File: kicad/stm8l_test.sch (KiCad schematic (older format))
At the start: 60 parts, among them J1 Conn_01x04, Q1 SI2365EDS-T1-GE3, Q2 2N7002, Q3 SI2365EDS-T1-GE3, Q4 SI2365EDS-T1-GE3, Q5 SI2365EDS-T1-GE3, Q6 SI2365EDS-T1-GE3, Q7 SI2365EDS-T1-GE3, Q8 SI2365EDS-T1-GE3, SW1 prog_sw, SW2 SW_Push, SW3 Rotary_Encoder_Switch, U1 BD70522GUL-E2, U2 STM8L101F3P

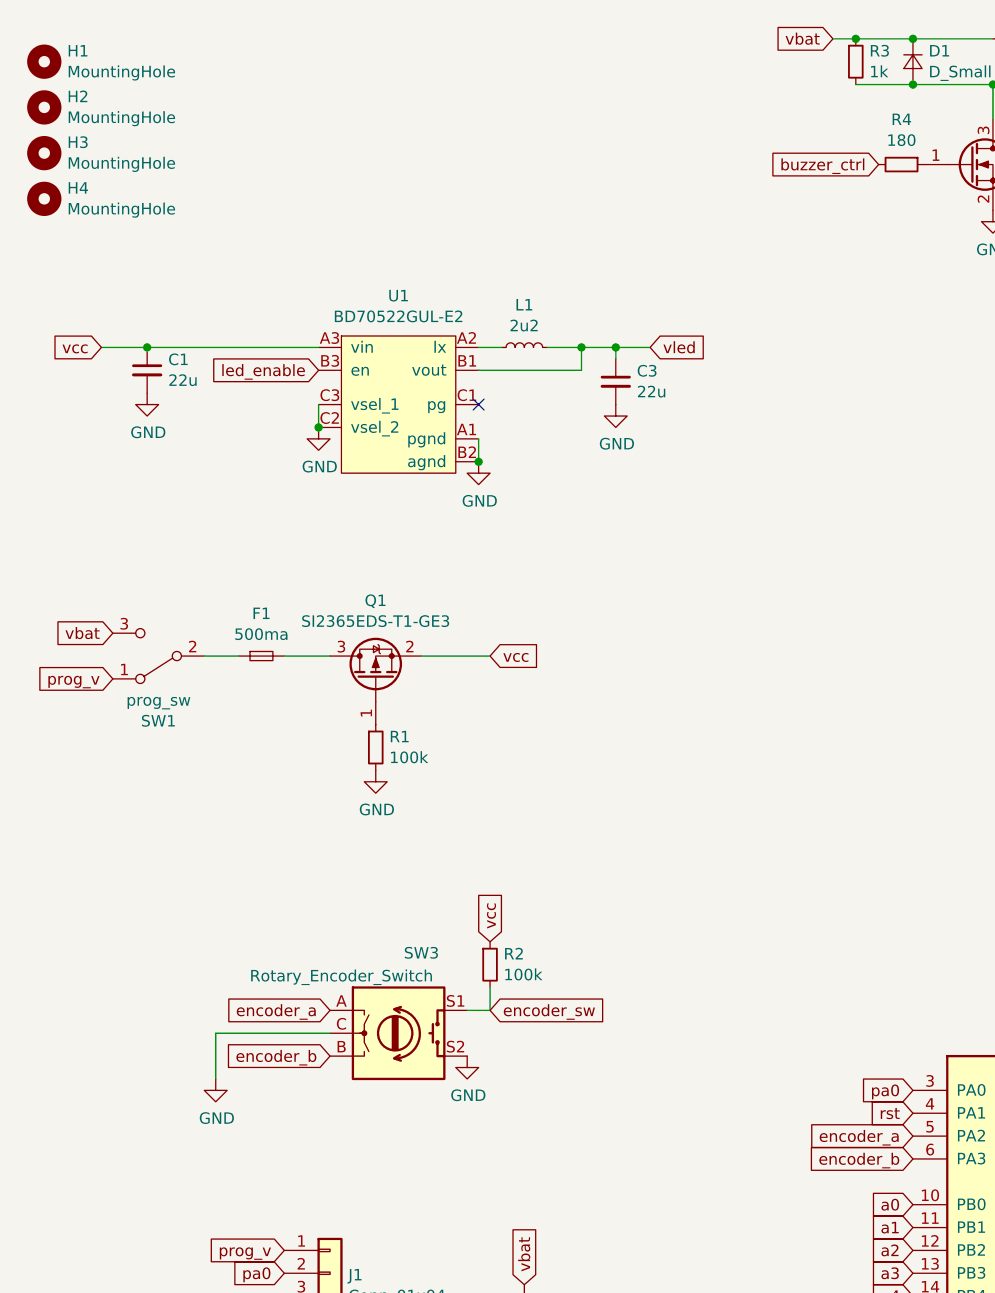
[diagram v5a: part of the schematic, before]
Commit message: Leds and buzzer works
added debounce caps
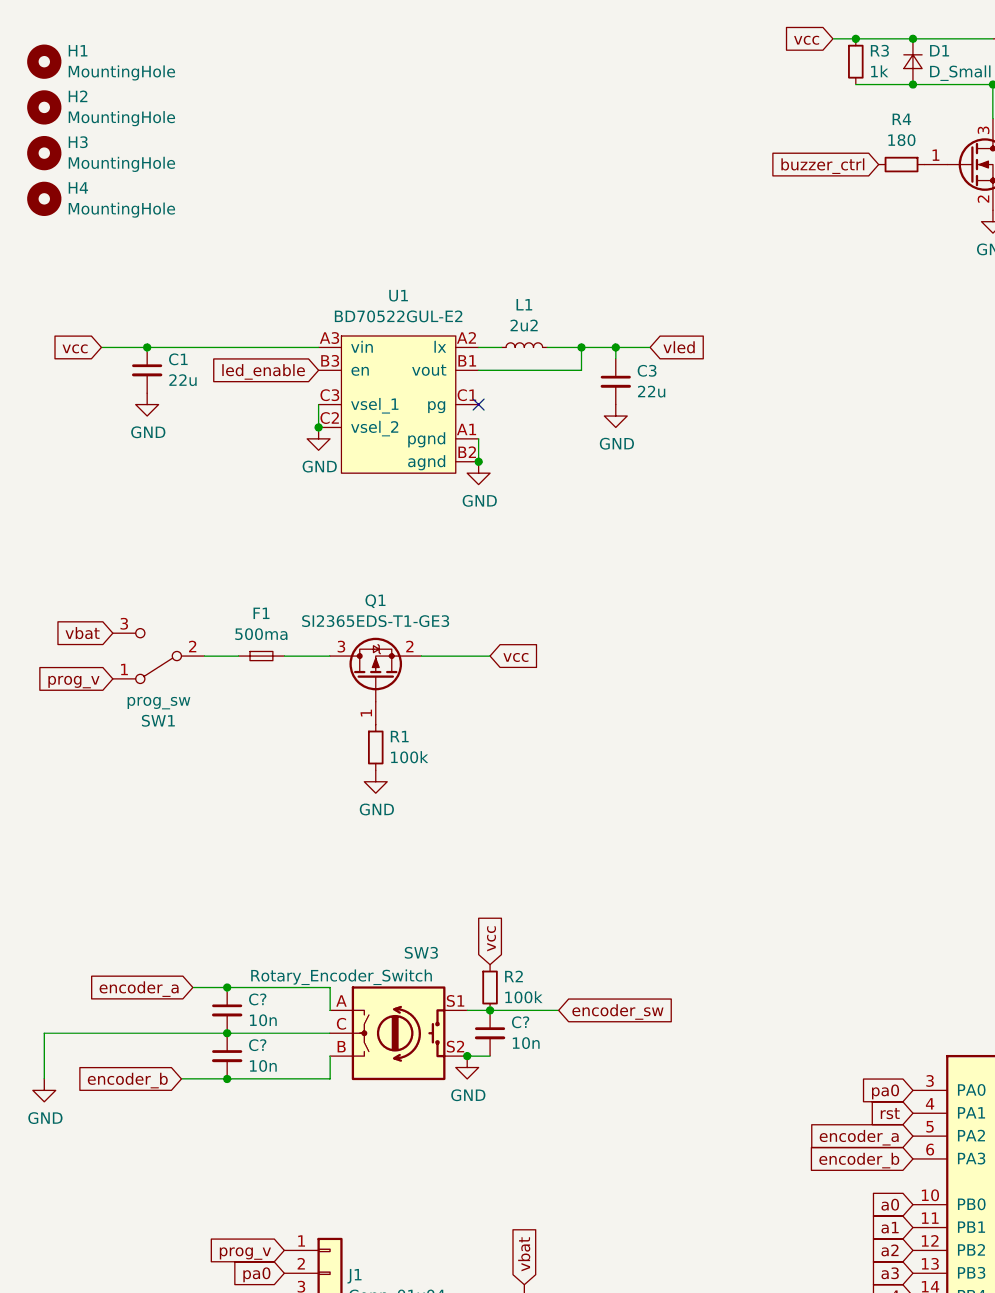
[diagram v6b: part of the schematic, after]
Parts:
- added C? (x3): 10n, symbol Device:C_Small
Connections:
- net GND: now also C?.1, C?.2, C?.2
- net encoder_a: now also C?.1
- net encoder_b: now also C?.2
- net encoder_sw: now also C?.1
- net vbat: no longer BZ1.1 (-), D1.1 (K), R3.1
- net vcc: now also BZ1.1 (-), D1.1 (K), R3.1
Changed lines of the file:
@@
 L power:GND #PWR02
 U 1 1 60746B0D
-P 1950 5250
-F 0 "#PWR02" H 1950 5000 50  0001 C CNN
-F 1 "GND" H 1955 5077 50  0000 C CNN
-F 2 "" H 1950 5250 50  0001 C CNN
-F 3 "" H 1950 5250 50  0001 C CNN
-	1    1950 5250
-	1    0    0    -1
-$EndComp
-Text GLabel 2450 5150 0    50   Input ~ 0
+P 1200 5250
+F 0 "#PWR02" H 1200 5000 50  0001 C CNN
+F 1 "GND" H 1205 5077 50  0000 C CNN
+F 2 "" H 1200 5250 50  0001 C CNN
+F 3 "" H 1200 5250 50  0001 C CNN
+	1    1200 5250
+	1    0    0    -1
+$EndComp
+Text GLabel 1800 5250 0    50   Input ~ 0
 encoder_b
-Text GLabel 2450 4950 0    50   Input ~ 0
+Text GLabel 1850 4850 0    50   Input ~ 0
 encoder_a
 Wire Wire Line
-	2450 5050 1950 5050
-Wire Wire Line
-	1950 5050 1950 5250
+	1200 5050 1200 5250
 $Comp
 L Device:Buzzer BZ1
@@
 	1    0    0    -1
 $EndComp
-Text GLabel 4650 700  0    50   Input ~ 0
-vbat
 Connection ~ 7900 1800
 Wire Wire Line
@@
 Wire Wire Line
 	6600 700  6800 700
-$Comp
-L Device:R_Small R2
-U 1 1 60B9FE81
-P 3150 4750
-F 0 "R2" H 3209 4796 50  0000 L CNN
-F 1 "100k" H 3209 4705 50  0000 L CNN
-F 2 "Resistor_SMD:R_0603_1608Metric_Pad1.05x0.95mm_HandSolder" H 3150 4750 50  0001 C CNN
-F 3 "~" H 3150 4750 50  0001 C CNN
-	1    3150 4750
-	1    0    0    -1
-$EndComp
-Text GLabel 3150 4650 1    50   Input ~ 0
-vcc
-Wire Wire Line
-	3150 4850 3150 4950
-Wire Wire Line
-	3150 4950 3050 4950
-Text GLabel 3150 4950 2    50   Input ~ 0
-encoder_sw
 Text GLabel 5000 6400 0    50   Input ~ 0
 encoder_sw
@@
 Wire Wire Line
 	2850 3400 3150 3400
+$Comp
+L Device:C_Small C?
+U 1 1 61046CCB
+P 2000 4950
+F 0 "C?" H 2092 4996 50  0000 L CNN
+F 1 "10n" H 2092 4905 50  0000 L CNN
+F 2 "" H 2000 4950 50  0001 C CNN
+F 3 "~" H 2000 4950 50  0001 C CNN
+	1    2000 4950
+	1    0    0    -1
+$EndComp
+$Comp
+L Device:C_Small C?
+U 1 1 61057664
+P 2000 5150
+F 0 "C?" H 2092 5196 50  0000 L CNN
+F 1 "10n" H 2092 5105 50  0000 L CNN
+F 2 "" H 2000 5150 50  0001 C CNN
+F 3 "~" H 2000 5150 50  0001 C CNN
+	1    2000 5150
+	1    0    0    -1
+$EndComp
+Wire Wire Line
+	2000 5050 2450 5050
+Connection ~ 2000 5050
+Wire Wire Line
+	1800 5250 2000 5250
+Wire Wire Line
+	2450 5250 2450 5150
+Connection ~ 2000 5250
+Wire Wire Line
+	2000 5250 2450 5250
+Wire Wire Line
+	2450 4950 2450 4850
+Wire Wire Line
+	2450 4850 2000 4850
+Connection ~ 2000 4850
+Wire Wire Line
+	2000 4850 1850 4850
+Text GLabel 3450 4950 2    50   Input ~ 0
+encoder_sw
+Wire Wire Line
+	1200 5050 2000 5050
+$Comp
+L Device:R_Small R2
+U 1 1 6108AE34
+P 3150 4850
+F 0 "R2" H 3209 4896 50  0000 L CNN
+F 1 "100k" H 3209 4805 50  0000 L CNN
+F 2 "Resistor_SMD:R_0603_1608Metric_Pad1.05x0.95mm_HandSolder" H 3150 4850 50  0001 C CNN
+F 3 "~" H 3150 4850 50  0001 C CNN
+	1    3150 4850
+	1    0    0    -1
+$EndComp
+Text GLabel 3150 4750 1    50   Input ~ 0
+vcc
+Text GLabel 4650 700  0    50   Input ~ 0
+vcc
+$Comp
+L Device:C_Small C?
+U 1 1 61091BE0
+P 3150 5050
+F 0 "C?" H 3242 5096 50  0000 L CNN
+F 1 "10n" H 3242 5005 50  0000 L CNN
+F 2 "" H 3150 5050 50  0001 C CNN
+F 3 "~" H 3150 5050 50  0001 C CNN
+	1    3150 5050
+	1    0    0    -1
+$EndComp
+Wire Wire Line
+	3050 4950 3150 4950
+Connection ~ 3150 4950
+Wire Wire Line
+	3150 5150 3050 5150
+Connection ~ 3050 5150
+Wire Wire Line
+	3150 4950 3450 4950
 $EndSCHEMATC
